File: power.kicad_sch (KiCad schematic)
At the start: 11 parts, among them Q1 IRLZ44N, U4 L78L05_SOT89

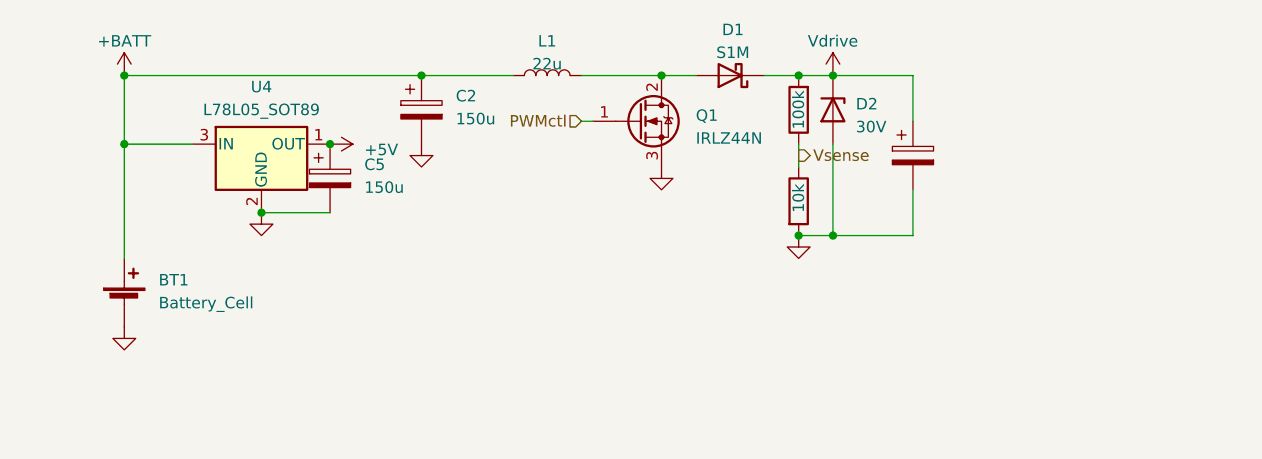
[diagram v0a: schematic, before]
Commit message: Add boost IC
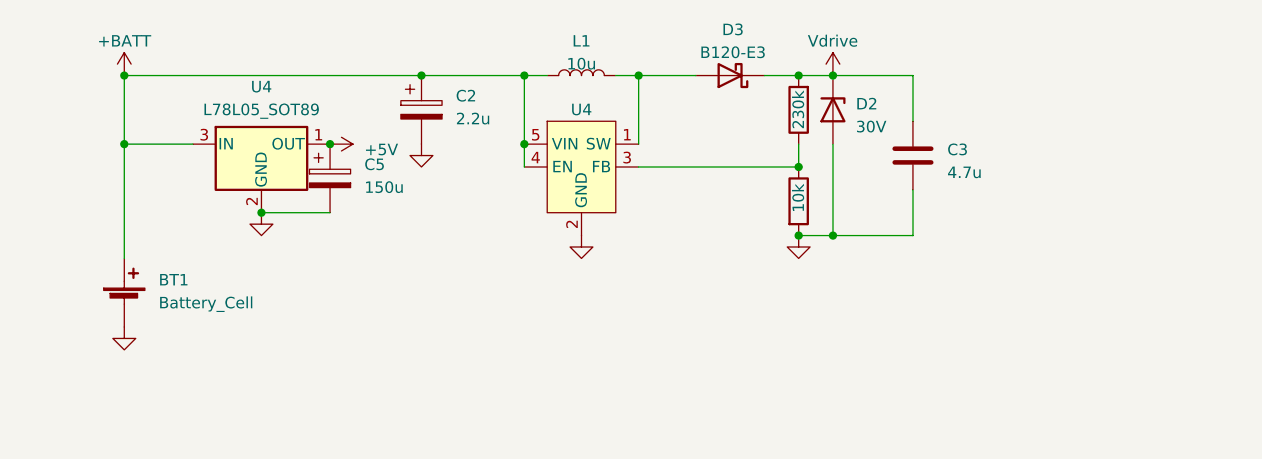
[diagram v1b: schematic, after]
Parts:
- removed C1: C_Polarized, Capacitor_THT:CP_Radial_D4.0mm_P2.00mm, symbol Device:C_Polarized
- removed D1: S1M, Diode_SMD:D_SMA, symbol Diode:B220
- removed Q1: IRLZ44N, Package_TO_SOT_SMD:SOT-89-3_Handsoldering, symbol Transistor_FET:IRLZ44N
- added C3: 4.7u, Capacitor_SMD:C_1206_3216Metric_Pad1.33x1.80mm_HandSolder, symbol Device:C
- added D3: B120-E3, Diode_SMD:D_SMA_Handsoldering, symbol Diode:B120-E3
- added U4: ~, Package_TO_SOT_SMD:SOT-23-5_HandSoldering, symbol custom_symbols:MIC2288
- C2: value 150u -> 2.2u; footprint Capacitor_THT:CP_Radial_D4.0mm_P1.50mm -> Capacitor_SMD:C_1206_3216Metric_Pad1.33x1.80mm_HandSolder
- L1: value 22u -> 10u
- R17: value 100k -> 230k
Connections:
- net +BATT: now also U4.4 (EN), U4.5 (VIN)
- net GND: now also C3.2, U4.2 (GND)
- net Vdrive: now also C3.1, D3.1 (K)
- net at L1.2: now also D3.2 (A), U4.1 (SW)
- net Vsense: no longer names the net of R16.1, R17.1
- net Vsense: now also U4.3 (FB)
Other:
- moved on the sheet: L1

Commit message: First production prototype
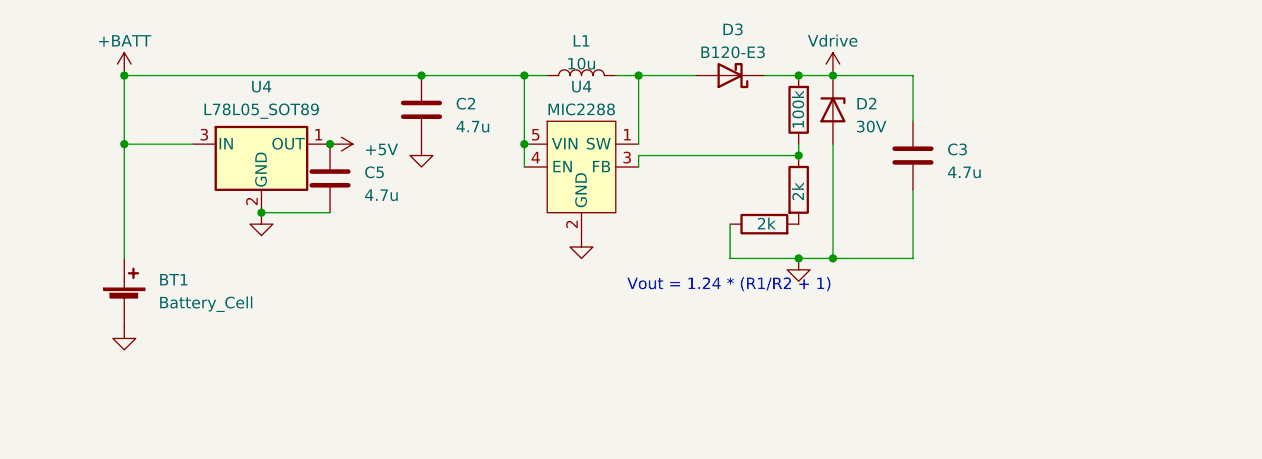
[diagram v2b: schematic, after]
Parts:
- removed C2: 2.2u, Capacitor_SMD:C_1206_3216Metric_Pad1.33x1.80mm_HandSolder, symbol Device:C_Polarized
- removed C5: 150u, Capacitor_THT:CP_Radial_D4.0mm_P1.50mm, symbol Device:C_Polarized
- added C2, C5: 4.7u, Capacitor_SMD:C_1206_3216Metric_Pad1.33x1.80mm_HandSolder, symbol Device:C
- added R16: 2k, Resistor_SMD:R_1206_3216Metric_Pad1.30x1.75mm_HandSolder, symbol Device:R
- BT1: footprint Connector_PinHeader_1.27mm:PinHeader_1x02_P1.27mm_Vertical -> Connector_PinSocket_1.27mm:PinSocket_1x02_P1.27mm_Vertical
- D2: footprint Diode_SMD:D_1206_3216Metric_Pad1.42x1.75mm_HandSolder -> Diode_SMD:D_SOD-123
- D3: footprint Diode_SMD:D_SMA_Handsoldering -> Diode_SMD:D_SOD-123
- L1: footprint Inductor_SMD_Wurth:L_Wurth_WE-LQSH-3012 -> Inductor_SMD:L_Coilcraft_XAL4030-XXX
- R16: value 10k -> 2k
- R17: value 230k -> 100k
- U4: value ~ -> MIC2288
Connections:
- net +5V: now also C5.1
- net +BATT: now also C2.1
- net GND: now also C2.2, C5.2, R16.1; no longer R16.2
- new net: R16.2, R16.2
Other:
- note added: "Vout = 1.24 * (R1/R2 + 1)"

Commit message: Prod 1a
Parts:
- BT1: footprint Connector_PinSocket_1.27mm:PinSocket_1x02_P1.27mm_Vertical -> Connector_PinHeader_2.54mm:PinHeader_1x02_P2.54mm_Vertical
- U4: footprint Package_TO_SOT_SMD:SOT-89-3 -> Package_TO_SOT_SMD:TO-252-2
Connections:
- net +5V: now also U4.3 (OUT); no longer U4.1 (OUT)
- net +BATT: now also U4.1 (IN); no longer U4.3 (IN)
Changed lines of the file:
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@@
       (effects (font (size 1.27 1.27)) (justify left))
     )
-    (property "Footprint" "Connector_PinSocket_1.27mm:PinSocket_1x02_P1.27mm_Vertical" (at 97.79 101.346 90)
+    (property "Footprint" "Connector_PinHeader_2.54mm:PinHeader_1x02_P2.54mm_Vertical" (at 97.79 101.346 90)
       (effects (font (size 1.27 1.27)) hide)
     )
@@
       (effects (font (size 1.27 1.27)))
     )
-    (property "Footprint" "Package_TO_SOT_SMD:SOT-89-3" (at 113.03 80.01 0)
+    (property "Footprint" "Package_TO_SOT_SMD:TO-252-2" (at 113.03 80.01 0)
       (effects (font (size 1.27 1.27) italic) hide)
     )
@@
       (effects (font (size 1.27 1.27)) hide)
     )
-    (pin "1")
-    (pin "2")
     (pin "3")
+    (pin "2")
+    (pin "1")
     (instances
       (project "locator_beacon"
@@
     )
     (pin "1")
+    (pin "2")
     (pin "3")
-    (pin "2")
     (pin "4")
     (pin "5")

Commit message: Work
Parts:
- removed D2: 30V, Diode_SMD:D_SOD-123, symbol Device:D_Zener
- removed U4: L78L05_SOT89, Package_TO_SOT_SMD:TO-252-2, symbol Regulator_Linear:L78L05_SOT89
- added C4: 4.7u, Capacitor_SMD:C_1206_3216Metric_Pad1.33x1.80mm_HandSolder, symbol Device:C
- added L1: 4.7u, Inductor_SMD:L_Coilcraft_XAL4030-XXX, symbol Device:L
- added U6: XC9140, Package_SO:TSOP-5_1.65x3.05mm_P0.95mm, symbol custom_symbols:XC9140
- C5: value 4.7u -> 10u
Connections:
- net +5V: now also U6.4 (V_{OUT})
- net +BATT: now also C4.1, L1.1, U6.1 (CE), U6.3 (V_{BAT})
- net GND: now also C4.2, U6.2 (GND)
- new net: L1.2, U6.5 (L_{x})
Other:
- moved on the sheet: C2, C5

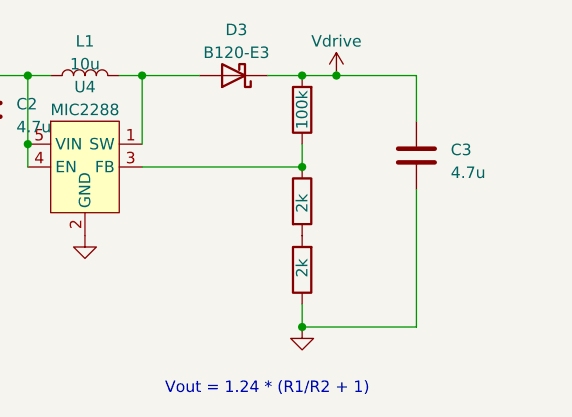
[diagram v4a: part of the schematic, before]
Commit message: Basic Class D amp
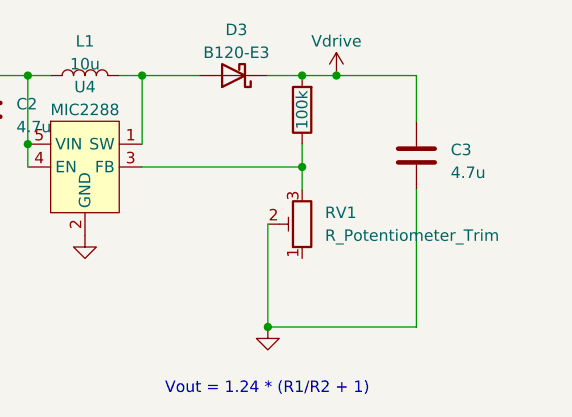
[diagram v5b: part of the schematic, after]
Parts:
- removed R16 (x2): 2k, Resistor_SMD:R_1206_3216Metric_Pad1.30x1.75mm_HandSolder, symbol Device:R
- added RV1: R_Potentiometer_Trim, custom:trimpot, symbol Device:R_Potentiometer_Trim
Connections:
- net GND: now also RV1.2
- net at R17.1, U4.3 (FB): now also RV1.3
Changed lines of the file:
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@@
   (junction (at 176.53 77.47) (diameter 0) (color 0 0 0 0)
   )
+  (junction (at 97.79 77.47) (diameter 0) (color 0 0 0 0)
+  )
+  (junction (at 101.6 85.09) (diameter 0) (color 0 0 0 0)
+  )
   (junction (at 172.72 87.63) (diameter 0) (color 0 0 0 0)
   )
-  (junction (at 97.79 77.47) (diameter 0) (color 0 0 0 0)
-  )
-  (junction (at 101.6 85.09) (diameter 0) (color 0 0 0 0)
-  )
   (junction (at 97.79 85.09) (diameter 0) (color 0 0 0 0)
   )
+  (junction (at 168.91 105.41) (diameter 0) (color 0 0 0 0)
+  )
   (junction (at 123.19 92.71) (diameter 0) (color 0 0 0 0)
   )
@@
   (junction (at 137.16 77.47) (diameter 0) (color 0 0 0 0)
   )
-  (junction (at 172.72 105.41) (diameter 0) (color 0 0 0 0)
-  )
   (wire (pts (xy 154.94 77.47) (xy 161.29 77.47))
     (stroke (width 0) (type default))
@@
     (stroke (width 0) (type default))
   )
+  (wire (pts (xy 168.91 105.41) (xy 185.42 105.41))
+    (stroke (width 0) (type default))
+  )
   (wire (pts (xy 154.94 87.63) (xy 172.72 87.63))
     (stroke (width 0) (type default))
   )
-  (wire (pts (xy 172.72 102.87) (xy 172.72 105.41))
+  (wire (pts (xy 168.91 93.98) (xy 168.91 105.41))
     (stroke (width 0) (type default))
   )
@@
     (stroke (width 0) (type default))
   )
-  (wire (pts (xy 172.72 105.41) (xy 185.42 105.41))
-    (stroke (width 0) (type default))
-  )
   (wire (pts (xy 142.24 77.47) (xy 144.78 77.47))
     (stroke (width 0) (type default))
   )
   (wire (pts (xy 152.4 77.47) (xy 154.94 77.47))
+    (stroke (width 0) (type default))
+  )
+  (wire (pts (xy 172.72 87.63) (xy 172.72 90.17))
     (stroke (width 0) (type default))
   )
@@
     )
   )
-  (symbol (lib_id "Device:R") (at 172.72 91.44 0) (unit 1)
-    (in_bom yes) (on_board yes) (dnp no)
-    (property "Reference" "R16" (at 175.26 90.805 0)
-      (effects (font (size 1.27 1.27)) (justify left) hide)
-    )
-    (property "Value" "2k" (at 172.72 92.71 90)
-      (effects (font (size 1.27 1.27)) (justify left))
-    )
-    (property "Footprint" "Resistor_SMD:R_1206_3216Metric_Pad1.30x1.75mm_HandSolder" (at 170.942 91.44 90)
-      (effects (font (size 1.27 1.27)) hide)
-    )
-    (property "Datasheet" "~" (at 172.72 91.44 0)
-      (effects (font (size 1.27 1.27)) hide)
-    )
-    (pin "1")
-    (pin "2")
-    (instances
-      (project "locator_beacon"
-        (path "/2e37f9ca-1f81-48a3-bbbb-9eab5c177622"
-          (reference "R16") (unit 1)
-        )
-        (path "/2e37f9ca-1f81-48a3-bbbb-9eab5c177622/45852106-87c2-4e1d-b1b1-72b985aa268b"
-          (reference "R15") (unit 1)
+  (symbol (lib_id "Device:R_Potentiometer_Trim") (at 172.72 93.98 180) (unit 1)
+    (in_bom yes) (on_board yes) (dnp no) (fields_autoplaced)
+    (property "Reference" "RV1" (at 175.26 92.71 0)
+      (effects (font (size 1.27 1.27)) (justify right))
+    )
+    (property "Value" "R_Potentiometer_Trim" (at 175.26 95.25 0)
+      (effects (font (size 1.27 1.27)) (justify right))
+    )
+    (property "Footprint" "custom:trimpot" (at 172.72 93.98 0)
+      (effects (font (size 1.27 1.27)) hide)
+    )
+    (property "Datasheet" "~" (at 172.72 93.98 0)
+      (effects (font (size 1.27 1.27)) hide)
+    )
+    (pin "1")
+    (pin "2")
+    (pin "3")
+    (instances
+      (project "locator_beacon"
+        (path "/2e37f9ca-1f81-48a3-bbbb-9eab5c177622/45852106-87c2-4e1d-b1b1-72b985aa268b"
+          (reference "RV1") (unit 1)
         )
       )
@@
         (path "/2e37f9ca-1f81-48a3-bbbb-9eab5c177622/45852106-87c2-4e1d-b1b1-72b985aa268b"
           (reference "C3") (unit 1)
-        )
-      )
-    )
-  )
-  (symbol (lib_id "Device:R") (at 172.72 99.06 180) (unit 1)
-    (in_bom yes) (on_board yes) (dnp no)
-    (property "Reference" "R16" (at 170.18 99.695 0)
-      (effects (font (size 1.27 1.27)) (justify left) hide)
-    )
-    (property "Value" "2k" (at 172.72 97.79 90)
-      (effects (font (size 1.27 1.27)) (justify left))
-    )
-    (property "Footprint" "Resistor_SMD:R_1206_3216Metric_Pad1.30x1.75mm_HandSolder" (at 174.498 99.06 90)
-      (effects (font (size 1.27 1.27)) hide)
-    )
-    (property "Datasheet" "~" (at 172.72 99.06 0)
-      (effects (font (size 1.27 1.27)) hide)
-    )
-    (pin "1")
-    (pin "2")
-    (instances
-      (project "locator_beacon"
-        (path "/2e37f9ca-1f81-48a3-bbbb-9eab5c177622"
-          (reference "R16") (unit 1)
-        )
-        (path "/2e37f9ca-1f81-48a3-bbbb-9eab5c177622/45852106-87c2-4e1d-b1b1-72b985aa268b"
-          (reference "R18") (unit 1)
         )
       )
@@
     )
   )
-  (symbol (lib_id "power:GND") (at 172.72 105.41 0) (unit 1)
-    (in_bom yes) (on_board yes) (dnp no) (fields_autoplaced)
-    (property "Reference" "#PWR011" (at 172.72 111.76 0)
-      (effects (font (size 1.27 1.27)) hide)
-    )
-    (property "Value" "GND" (at 172.72 110.49 0)
-      (effects (font (size 1.27 1.27)) hide)
-    )
-    (property "Footprint" "" (at 172.72 105.41 0)
-      (effects (font (size 1.27 1.27)) hide)
-    )
-    (property "Datasheet" "" (at 172.72 105.41 0)
-      (effects (font (size 1.27 1.27)) hide)
-    )
+  (symbol (lib_id "power:GND") (at 168.91 105.41 0) (unit 1)
+    (in_bom yes) (on_board yes) (dnp no) (fields_autoplaced)
+    (property "Reference" "#PWR011" (at 168.91 111.76 0)
+      (effects (font (size 1.27 1.27)) hide)
+    )
+    (property "Value" "GND" (at 168.91 110.49 0)
+      (effects (font (size 1.27 1.27)) hide)
+    )
+    (property "Footprint" "" (at 168.91 105.41 0)
+      (effects (font (size 1.27 1.27)) hide)
+    )
+    (property "Datasheet" "" (at 168.91 105.41 0)
+      (effects (font (size 1.27 1.27)) hide)
+    )

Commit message: Seems reasonable
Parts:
- removed C4: 4.7u, Capacitor_SMD:C_1206_3216Metric_Pad1.33x1.80mm_HandSolder, symbol Device:C
- removed C5: 10u, Capacitor_SMD:C_1206_3216Metric_Pad1.33x1.80mm_HandSolder, symbol Device:C
- removed L1: 4.7u, Inductor_SMD:L_Coilcraft_XAL4030-XXX, symbol Device:L
- removed R17: 100k, Resistor_SMD:R_1206_3216Metric_Pad1.30x1.75mm_HandSolder, symbol Device:R
- removed U4: MIC2288, Package_TO_SOT_SMD:SOT-23-5_HandSoldering, symbol custom_symbols:MIC2288
- removed U6: XC9140, Package_SO:TSOP-5_1.65x3.05mm_P0.95mm, symbol custom_symbols:XC9140
- added C1: C, Capacitor_SMD:C_0603_1608Metric, symbol Device:C_Polarized
- added J1: Conn_01x02, Connector_PinHeader_2.54mm:PinHeader_1x02_P2.54mm_Horizontal, symbol Connector_Generic:Conn_01x02
- added TP1: +V, TestPoint:TestPoint_Pad_D1.0mm, symbol Connector:TestPoint
- added U1: MC34063AD, Package_SO:SOIC-8_3.9x4.9mm_P1.27mm, symbol Regulator_Switching:MC34063AD
- C2: value 4.7u -> 1.5n; footprint Capacitor_SMD:C_1206_3216Metric_Pad1.33x1.80mm_HandSolder -> Capacitor_SMD:C_0603_1608Metric
- C3: footprint Capacitor_SMD:C_1206_3216Metric_Pad1.33x1.80mm_HandSolder -> Capacitor_SMD:C_0603_1608Metric
- L1: footprint Inductor_SMD:L_Coilcraft_XAL4030-XXX -> Inductor_SMD:L_1008_2520Metric
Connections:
- net +BATT: now also C1.1, J1.2 (Pin_2), U1.6 (Vin), U1.7 (Ipk), U1.8 (DC); no longer C2.1
- net GND: now also RV1.1, C1.2, J1.1 (Pin_1), U1.2 (SwE), U1.4 (GND); no longer RV1.2
- net Vdrive: now also RV1.3, TP1.1
- net at D3.2 (A), L1.2: now also U1.1 (SwC)
- new net: C2.1, U1.3 (TC)
- new net: RV1.2, U1.5 (Vfb)
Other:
- note removed: "Vout = 1.24 * (R1/R2 + 1)"
- moved on the sheet: C2, C3, D3, L1, RV1

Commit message: Tweaks
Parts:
- removed C3: 4.7u, Capacitor_SMD:C_0603_1608Metric, symbol Device:C
- BT1: now left out of the parts list
- D3: value B120-E3 -> DSS16U
- L1: footprint Inductor_SMD:L_1008_2520Metric -> Inductor_SMD:L_1210_3225Metric
- RV1: value R_Potentiometer_Trim -> 100k; footprint custom:trimpot -> Potentiometer_SMD:Potentiometer_Bourns_3314J_Vertical
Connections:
- net GND: now also RV1.3; no longer RV1.1
- net Vdrive: now also RV1.1; no longer RV1.3
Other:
- moved on the sheet: RV1
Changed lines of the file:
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@@
+      (effects (font (size 1.27 1.27)) hide)
+    )
+    (property "Sim.Enable" "0" (at 151.13 97.79 0)
       (effects (font (size 1.27 1.27)) hide)
     )
@@
     )
   )
-  (symbol (lib_id "Device:R_Potentiometer_Trim") (at 187.96 105.41 180) (unit 1)
-    (in_bom yes) (on_board yes) (dnp no) (fields_autoplaced)
+  (symbol (lib_id "Device:R_Potentiometer_Trim") (at 187.96 105.41 0) (mirror y) (unit 1)
+    (in_bom yes) (on_board yes) (dnp no)
     (property "Reference" "RV1" (at 190.5 104.14 0)
       (effects (font (size 1.27 1.27)) (justify right))
     )
-    (property "Value" "R_Potentiometer_Trim" (at 190.5 106.68 0)
+    (property "Value" "100k" (at 190.5 106.68 0)
       (effects (font (size 1.27 1.27)) (justify right))
     )
-    (property "Footprint" "custom:trimpot" (at 187.96 105.41 0)
+    (property "Footprint" "Potentiometer_SMD:Potentiometer_Bourns_3314J_Vertical" (at 187.96 105.41 0)
       (effects (font (size 1.27 1.27)) hide)
     )
@@
   )
   (symbol (lib_id "Device:Battery_Cell") (at 120.65 110.49 0) (unit 1)
-    (in_bom yes) (on_board no) (dnp no)
+    (in_bom no) (on_board no) (dnp no)
     (property "Reference" "BT1" (at 113.03 109.22 0)
       (effects (font (size 1.27 1.27)) (justify left) hide)
@@
       (effects (font (size 1.27 1.27)))
     )
-    (property "Value" "B120-E3" (at 179.3875 74.93 0)
+    (property "Value" "DSS16U" (at 179.3875 74.93 0)
       (effects (font (size 1.27 1.27)))
     )
@@
         (path "/2e37f9ca-1f81-48a3-bbbb-9eab5c177622/45852106-87c2-4e1d-b1b1-72b985aa268b"
           (reference "D3") (unit 1)
-        )
-      )
-    )
-  )
-  (symbol (lib_id "Device:C") (at 199.39 86.36 0) (unit 1)
-    (in_bom yes) (on_board yes) (dnp no) (fields_autoplaced)
-    (property "Reference" "C3" (at 203.2 85.725 0)
-      (effects (font (size 1.27 1.27)) (justify left))
-    )
-    (property "Value" "4.7u" (at 203.2 88.265 0)
-      (effects (font (size 1.27 1.27)) (justify left))
-    )
-    (property "Footprint" "Capacitor_SMD:C_0603_1608Metric" (at 200.3552 90.17 0)
-      (effects (font (size 1.27 1.27)) hide)
-    )
-    (property "Datasheet" "~" (at 199.39 86.36 0)
-      (effects (font (size 1.27 1.27)) hide)
-    )
-    (pin "1")
-    (pin "2")
-    (instances
-      (project "locator_beacon"
-        (path "/2e37f9ca-1f81-48a3-bbbb-9eab5c177622/45852106-87c2-4e1d-b1b1-72b985aa268b"
-          (reference "C3") (unit 1)
         )
       )
@@
       (effects (font (size 1.27 1.27)))
     )
-    (property "Footprint" "Inductor_SMD:L_1008_2520Metric" (at 167.64 77.47 0)
-      (effects (font (size 1.27 1.27)) hide)
-    )
+    (property "Footprint" "Inductor_SMD:L_1210_3225Metric" (at 167.64 77.47 0)
+      (effects (font (size 1.27 1.27)) hide)
+    )

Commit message: Tweaks
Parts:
- J1, TP1: now left out of the parts list
- L1: footprint Inductor_SMD:L_1210_3225Metric -> Inductor_SMD:L_Taiyo-Yuden_MD-4040
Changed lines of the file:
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@@
+      (effects (font (size 1.27 1.27)) hide)
+    )
+    (property "Sim.Enable" "0" (at 120.65 110.49 0)
       (effects (font (size 1.27 1.27)) hide)
     )
@@
   )
   (symbol (lib_id "Connector:TestPoint") (at 199.39 77.47 0) (unit 1)
-    (in_bom yes) (on_board yes) (dnp no) (fields_autoplaced)
+    (in_bom no) (on_board yes) (dnp no) (fields_autoplaced)
     (property "Reference" "TP1" (at 201.93 72.898 0)
       (effects (font (size 1.27 1.27)) (justify left))
@@
     )
     (property "Datasheet" "~" (at 204.47 77.47 0)
+      (effects (font (size 1.27 1.27)) hide)
+    )
+    (property "Sim.Enable" "0" (at 199.39 77.47 0)
       (effects (font (size 1.27 1.27)) hide)
     )
@@
   )
   (symbol (lib_id "Connector_Generic:Conn_01x02") (at 101.6 110.49 180) (unit 1)
-    (in_bom yes) (on_board yes) (dnp no)
+    (in_bom no) (on_board yes) (dnp no)
     (property "Reference" "J1" (at 99.06 110.49 0)
       (effects (font (size 1.27 1.27)) (justify left))
@@
     )
     (property "Datasheet" "~" (at 101.6 110.49 0)
+      (effects (font (size 1.27 1.27)) hide)
+    )
+    (property "Sim.Enable" "0" (at 101.6 110.49 0)
       (effects (font (size 1.27 1.27)) hide)
     )
@@
       (effects (font (size 1.27 1.27)))
     )
-    (property "Footprint" "Inductor_SMD:L_1210_3225Metric" (at 167.64 77.47 0)
-      (effects (font (size 1.27 1.27)) hide)
-    )
+    (property "Footprint" "Inductor_SMD:L_Taiyo-Yuden_MD-4040" (at 167.64 77.47 0)
+      (effects (font (size 1.27 1.27)) hide)
+    )
